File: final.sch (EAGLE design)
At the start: 18 parts, among them M2 MOTOR10MM, M3 MOTOR10MM, Q1 500mA/300V

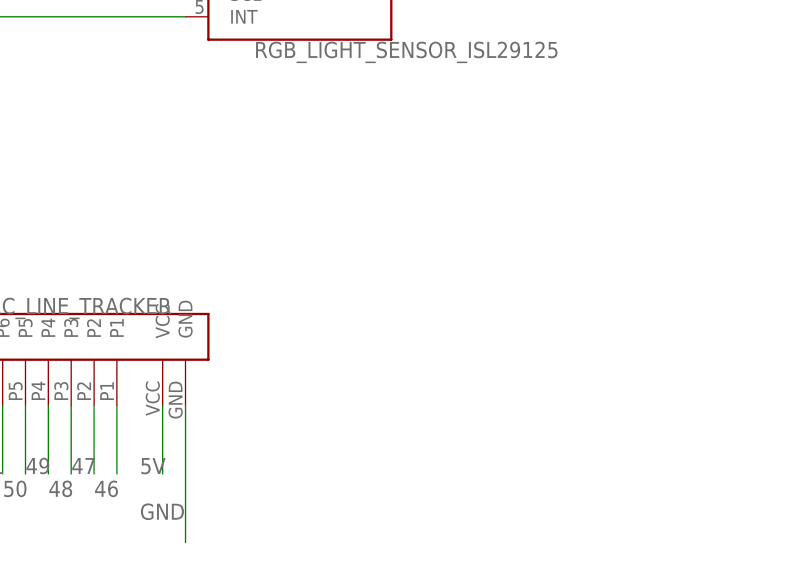
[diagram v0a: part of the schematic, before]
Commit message: Add Bumper Circuit Schematic
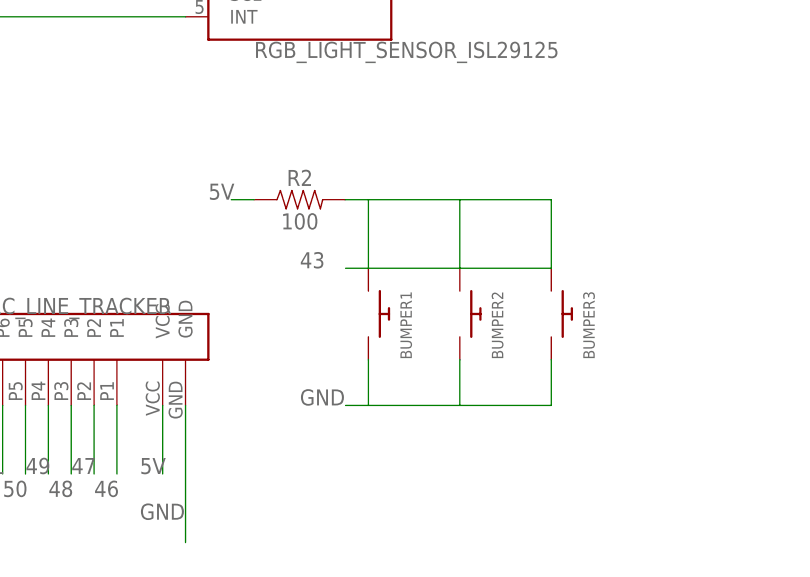
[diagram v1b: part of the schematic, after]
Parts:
- added BUMPER1, BUMPER2, BUMPER3: (no value), adafruit:SWITCH_PUSHBUTTONSOFTTOUCHSMD_SJ
- added R2: 100, SparkFun-Resistors:100OHM-HORIZ_KIT-1/4W-1%
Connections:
- new net 43: BUMPER1.P$1, BUMPER2.P$1, BUMPER3.P$1, R2.2
- net 5V: now also R2.1
- net GND: now also BUMPER1.P$2, BUMPER2.P$2, BUMPER3.P$2
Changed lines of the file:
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@@
 <?xml version="1.0" encoding="utf-8"?>
 <!DOCTYPE eagle SYSTEM "eagle.dtd">
-<eagle version="8.6.0">
+<eagle version="7.7.0">
 <drawing>
 <settings>
@@
 <part name="EMERGENCY" library="adafruit" deviceset="SWITCH_PUSHBUTTON" device="SOFTTOUCHSMD_SJ"/>
 <part name="U$1" library="custom" deviceset="HX711_CARRIER" device=""/>
+<part name="BUMPER1" library="adafruit" deviceset="SWITCH_PUSHBUTTON" device="SOFTTOUCHSMD_SJ"/>
+<part name="BUMPER2" library="adafruit" deviceset="SWITCH_PUSHBUTTON" device="SOFTTOUCHSMD_SJ"/>
+<part name="BUMPER3" library="adafruit" deviceset="SWITCH_PUSHBUTTON" device="SOFTTOUCHSMD_SJ"/>
+<part name="R2" library="SparkFun-Resistors" deviceset="100OHM" device="-HORIZ_KIT-1/4W-1%" value="100"/>
 </parts>
 <sheets>
@@
 <instance part="EMERGENCY" gate="G$1" x="20.32" y="106.68"/>
 <instance part="U$1" gate="G$1" x="-101.6" y="7.62"/>
+<instance part="BUMPER1" gate="G$1" x="60.96" y="-25.4" rot="R270"/>
+<instance part="BUMPER2" gate="G$1" x="71.12" y="-25.4" rot="R270"/>
+<instance part="BUMPER3" gate="G$1" x="81.28" y="-25.4" rot="R270"/>
+<instance part="R2" gate="G$1" x="53.34" y="-12.7"/>
 </instances>
 <busses>
@@
 <label x="-81.28" y="2.54" size="1.778" layer="95"/>
 </segment>
+<segment>
+<pinref part="BUMPER3" gate="G$1" pin="P$2"/>
+<wire x1="81.28" y1="-30.48" x2="81.28" y2="-35.56" width="0.1524" layer="91"/>
+<wire x1="81.28" y1="-35.56" x2="71.12" y2="-35.56" width="0.1524" layer="91"/>
+<pinref part="BUMPER1" gate="G$1" pin="P$2"/>
+<wire x1="71.12" y1="-35.56" x2="60.96" y2="-35.56" width="0.1524" layer="91"/>
+<wire x1="58.42" y1="-35.56" x2="60.96" y2="-35.56" width="0.1524" layer="91"/>
+<wire x1="60.96" y1="-35.56" x2="60.96" y2="-30.48" width="0.1524" layer="91"/>
+<pinref part="BUMPER2" gate="G$1" pin="P$2"/>
+<wire x1="71.12" y1="-30.48" x2="71.12" y2="-35.56" width="0.1524" layer="91"/>
+<label x="53.34" y="-35.56" size="1.778" layer="95"/>
+</segment>
 </net>
 <net name="BATT" class="0">
@@
 <junction x="-83.82" y="12.7"/>
 <label x="-81.28" y="12.7" size="1.778" layer="95"/>
+</segment>
+<segment>
+<pinref part="R2" gate="G$1" pin="1"/>
+<wire x1="48.26" y1="-12.7" x2="45.72" y2="-12.7" width="0.1524" layer="91"/>
+<label x="43.18" y="-12.7" size="1.778" layer="91"/>
 </segment>
 </net>
@@
 </segment>
 </net>
+<net name="43" class="0">
+<segment>
+<pinref part="BUMPER1" gate="G$1" pin="P$1"/>
+<wire x1="60.96" y1="-20.32" x2="58.42" y2="-20.32" width="0.1524" layer="91"/>
+<pinref part="BUMPER2" gate="G$1" pin="P$1"/>
+<wire x1="60.96" y1="-20.32" x2="71.12" y2="-20.32" width="0.1524" layer="91"/>
+<pinref part="BUMPER3" gate="G$1" pin="P$1"/>
+<wire x1="71.12" y1="-20.32" x2="81.28" y2="-20.32" width="0.1524" layer="91"/>
+<wire x1="81.28" y1="-20.32" x2="81.28" y2="-12.7" width="0.1524" layer="91"/>
+<wire x1="81.28" y1="-12.7" x2="71.12" y2="-12.7" width="0.1524" layer="91"/>
+<wire x1="71.12" y1="-12.7" x2="71.12" y2="-20.32" width="0.1524" layer="91"/>
+<wire x1="71.12" y1="-12.7" x2="60.96" y2="-12.7" width="0.1524" layer="91"/>
+<wire x1="60.96" y1="-12.7" x2="60.96" y2="-20.32" width="0.1524" layer="91"/>
+<wire x1="60.96" y1="-12.7" x2="58.42" y2="-12.7" width="0.1524" layer="91"/>
+<pinref part="R2" gate="G$1" pin="2"/>
+<label x="53.34" y="-20.32" size="1.778" layer="95"/>
+</segment>
+</net>
